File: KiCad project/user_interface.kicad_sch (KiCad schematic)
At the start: 11 parts, among them J4 B4B-XH-AM, J6 Conn_01x05, Q2 BC817, Q3 BC817, SW1 1101NE, SW2 1101NE

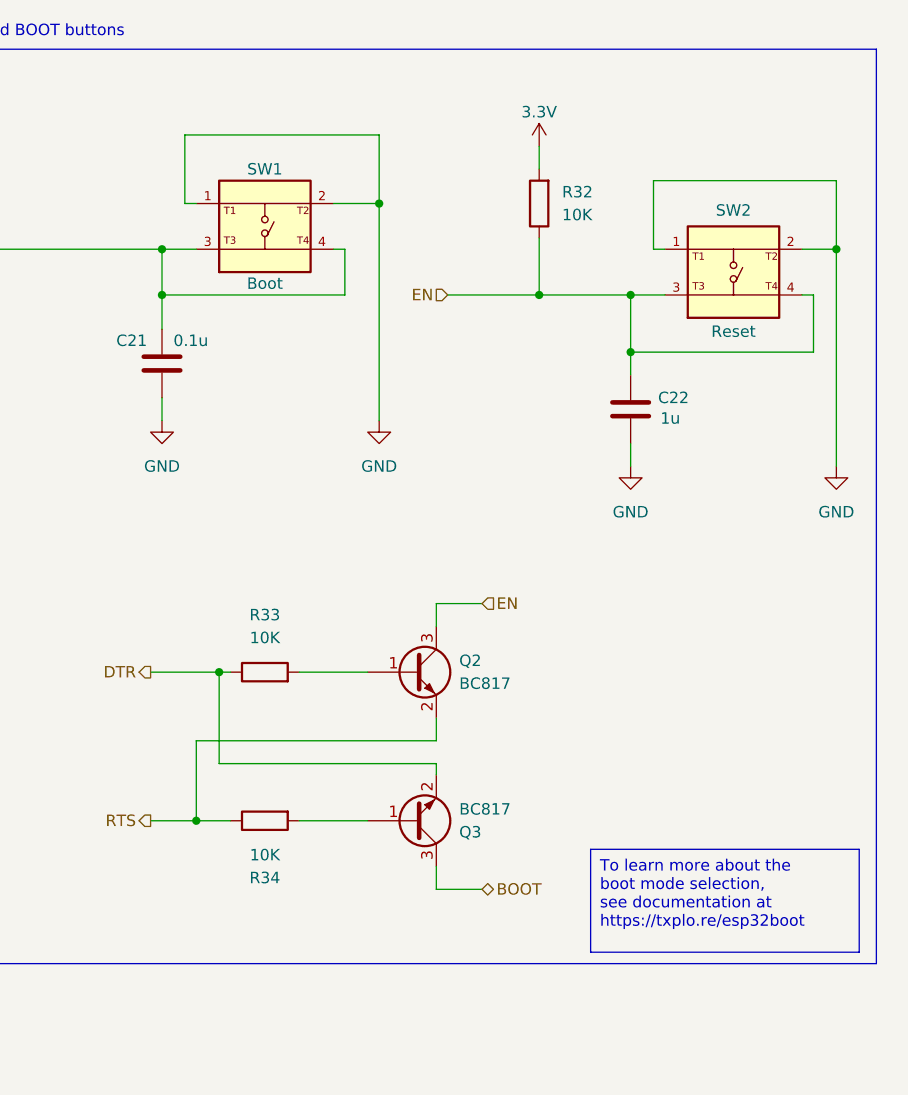
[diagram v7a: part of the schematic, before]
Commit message: Fixed and improved Schematic design:
* Changed the buttons
* Added a ferrite bead at the output of the charger to cut some possible noise.
* Changed the values of R30, R31 and C19, and i add a 100K trimmer to set the gain from 25x to 125x.
* Added C23, C24 and C25 in the photo sensor circuit
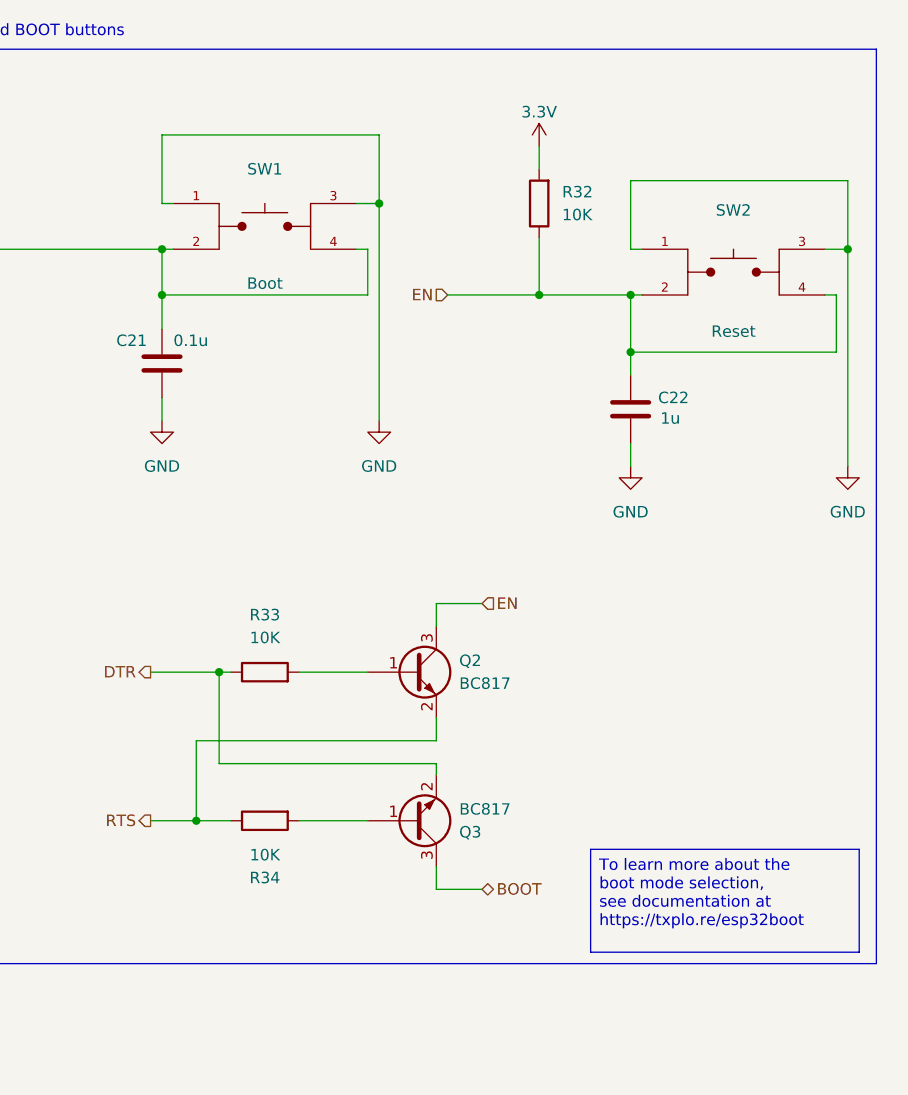
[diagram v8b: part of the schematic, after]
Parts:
- SW1, SW2: footprint Footprints:SW_USLPT2819DT2TR -> TL3305AF260QG:SW_TL3305AF260QG; symbol USLPT2819DT2TR:USLPT2819DT2TR -> TL3305AF260QG:TL3305AF260QG; Check_prices https://www.snapeda.com/parts/USLPT2819DT2TR/TE+Connectivit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 -> https://www.snapeda.com/parts/TL3305AF260QG/E-Switch/view-p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; Description_1 Tactile Switch SPST-NO Top Actuated Surface Mount -> Tactile Switch SPST-NO Top Actuated Surface Mount; MANUFACTURER TE CONNECTIVITY -> E-Switch; MAXIMUM_PACKAGE_HEIGHT (none) -> 3.8mm; MF TE Connectivity -> E-Switch; MP USLPT2819DT2TR -> TL3305AF260QG; PARTREV P -> C; Package None -> SMD-4 E-Switch; STANDARD Manufacturer Recommendations -> Manufacturer recommendations; SnapEDA_Link https://www.snapeda.com/parts/USLPT2819DT2TR/TE+Connectivit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 -> https://www.snapeda.com/parts/TL3305AF260QG/E-Switch/view-p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
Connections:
- net BOOT: now also SW1.2; no longer SW1.3
- net EN: now also SW2.2; no longer SW2.3
- net GND: now also SW1.3, SW2.3; no longer SW1.2, SW2.2
